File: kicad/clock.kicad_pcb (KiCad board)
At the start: 2 copper layers, 74 x 36 mm, 50 parts, among them P1 CONN_01X03, SW1 SWITCH_MIN, SW2 SWITCH_HR, U1 74LS90, U10 74LS247, U11 74LS73, U2 74LS90, U3 MAX6817, U4 74LS90, U5 74LS247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

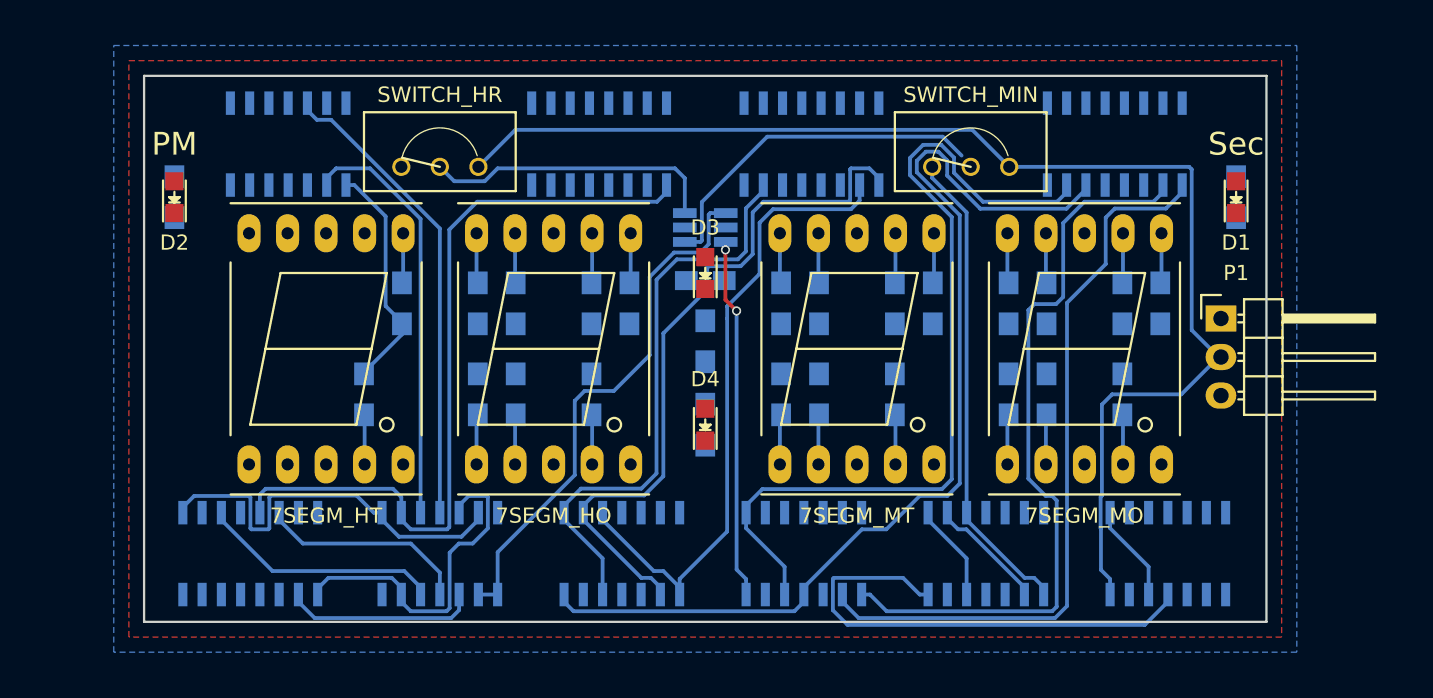
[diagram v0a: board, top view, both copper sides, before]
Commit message: Continue routing, add two layers
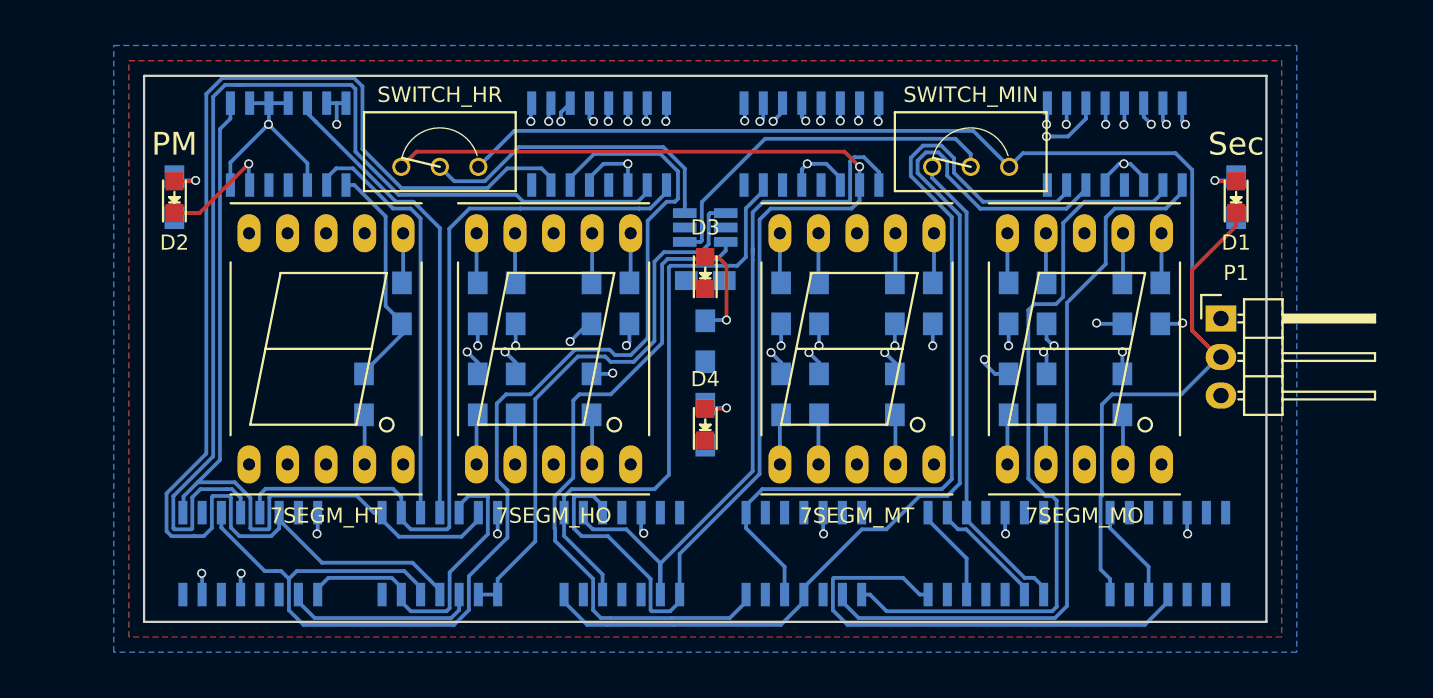
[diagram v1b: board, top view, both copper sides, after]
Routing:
- net /hoi2: track 0.00 -> 73.1 mm
- net /hoi0: track 14.4 -> 86.9 mm
- net /hoi3: track 15.9 -> 79.2 mm
- net VCC: track 0.00 -> 44.2 mm, vias 0 -> 15
- net /mti2: track 42.8 -> 84.2 mm, vias 0 -> 1
- net /hr_one_c: track 0.00 -> 36.5 mm, vias 0 -> 2
- net /min_ten_c: track 0.00 -> 33.1 mm, vias 0 -> 2
- net /min_one_c: track 0.00 -> 32.1 mm, vias 0 -> 2
- net /hr_one_g: track 0.00 -> 30.0 mm, vias 0 -> 2
- net /min_one_g: track 0.00 -> 29.6 mm, vias 0 -> 2
- net /min_ten_g: track 0.00 -> 28.3 mm, vias 0 -> 2
- net Net-(U11-Pad1): track 26.7 -> 54.1 mm
- net /hr_one_d: track 0.00 -> 27.0 mm, vias 0 -> 2
- net /min_ten_d: track 0.00 -> 25.1 mm, vias 0 -> 2
- net /min_ten_f: track 0.00 -> 24.9 mm, vias 0 -> 2
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- added copper zone on In1.Cu, net GND
- added copper zone on In2.Cu, net GND
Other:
- copper layers 2 -> 4

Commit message: Add bypass caps and route VCC
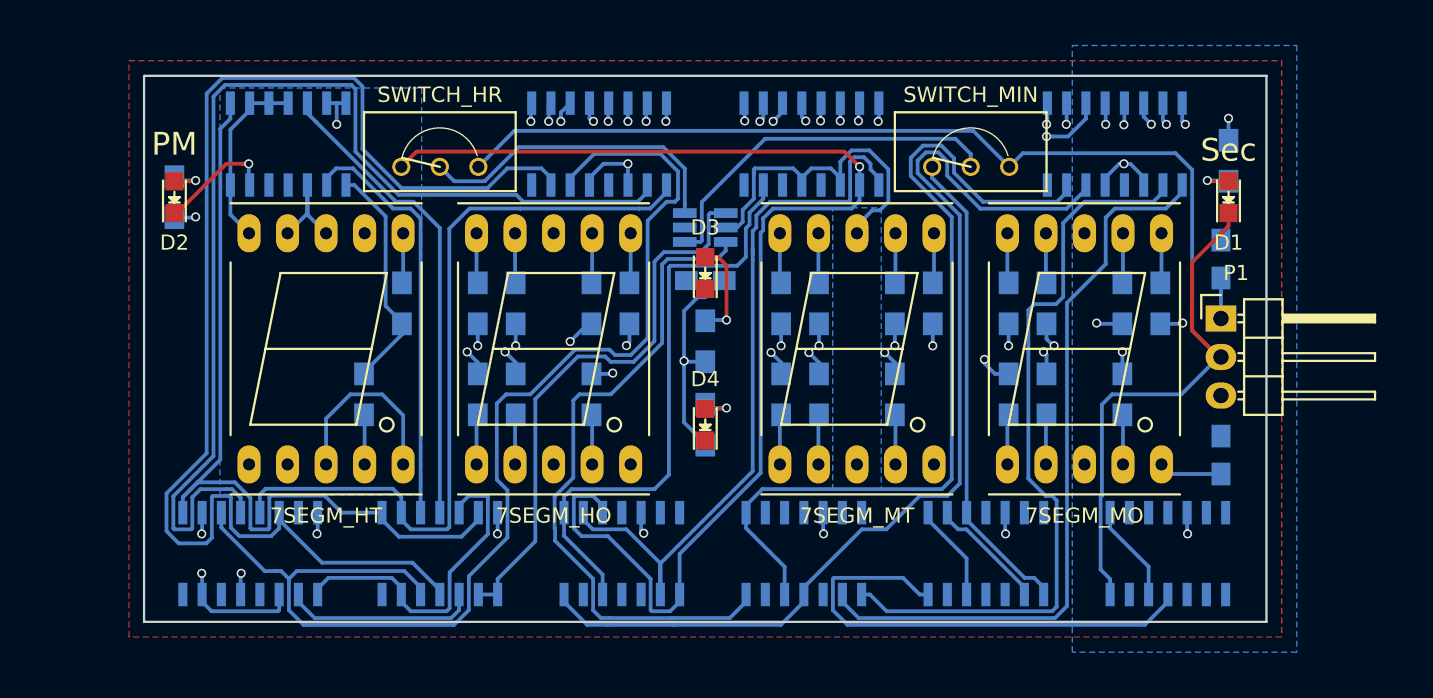
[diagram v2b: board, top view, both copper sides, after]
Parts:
- added C1: 22μF, Capacitors_SMD:C_0805_HandSoldering, B.Cu at (189.0, 103.0)
- added C2: 22μF, Capacitors_SMD:C_0805_HandSoldering, B.Cu at (189.0, 90.1)
- moved R1 2.45 mm to (189.5, 83.6), turned to 90 degrees
- moved D1 0.50 mm to (189.5, 86.0)
- renumbered C1 to C3, U8 to U7, U7 to U8
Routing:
- net VCC: track 44.2 -> 114.3 mm, vias 15 -> 17
- net /osc: track 96.5 -> 98.2 mm
- net Net-(U11-Pad1): track 54.1 -> 55.7 mm
- net /hoi0: track 86.9 -> 87.6 mm
- added copper zone on B.Cu, net VCC

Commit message: Complete layout, pass DRC, create gerbers
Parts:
- added REF**: MountingHole_3.2mm_M3, Mounting_Holes:MountingHole_3.2mm_M3, F.Cu at (194.5, 111.0)
- added REF**: MountingHole_3.2mm_M3, Mounting_Holes:MountingHole_3.2mm_M3, F.Cu at (116.0, 111.0)
- added REF**: MountingHole_3.2mm_M3, Mounting_Holes:MountingHole_3.2mm_M3, F.Cu at (116.0, 81.0)
- added REF**: MountingHole_3.2mm_M3, Mounting_Holes:MountingHole_3.2mm_M3, F.Cu at (194.5, 81.0)
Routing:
- net GND: track 1.41 -> 63.7 mm, vias 1 -> 14
- net /mti2: track 84.1 -> 91.8 mm
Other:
- board size 74 x 36 mm -> 86.5 x 38 mm
- net class Default: clearance 0.2 -> 0.16
- rule trace_clearance: 0.2 -> 0.16

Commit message: Add version and license silkscreen text
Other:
- board text added: "Click-Clock Board v0.1 GNU GPLv3"
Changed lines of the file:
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@@
     (links 179)
     (no_connects 0)
-    (area 106.482857 73 204.017143 119.000001)
+    (area 111.924999 76.924999 198.575001 115.075001)
     (thickness 1.6)
-    (drawings 18)
+    (drawings 19)
     (tracks 993)
     (zones 0)
@@
       (net 2 GND) (zone_connect 2))
   )
+  (gr_text "Click-Clock Board v0.1\nGNU GPLv3" (at 155 111) (layer F.SilkS)
+    (effects (font (size 1.5 1.5) (thickness 0.3)))
+  )
   (gr_line (start 116 77) (end 194.5 77) (angle 90) (layer Edge.Cuts) (width 0.15))

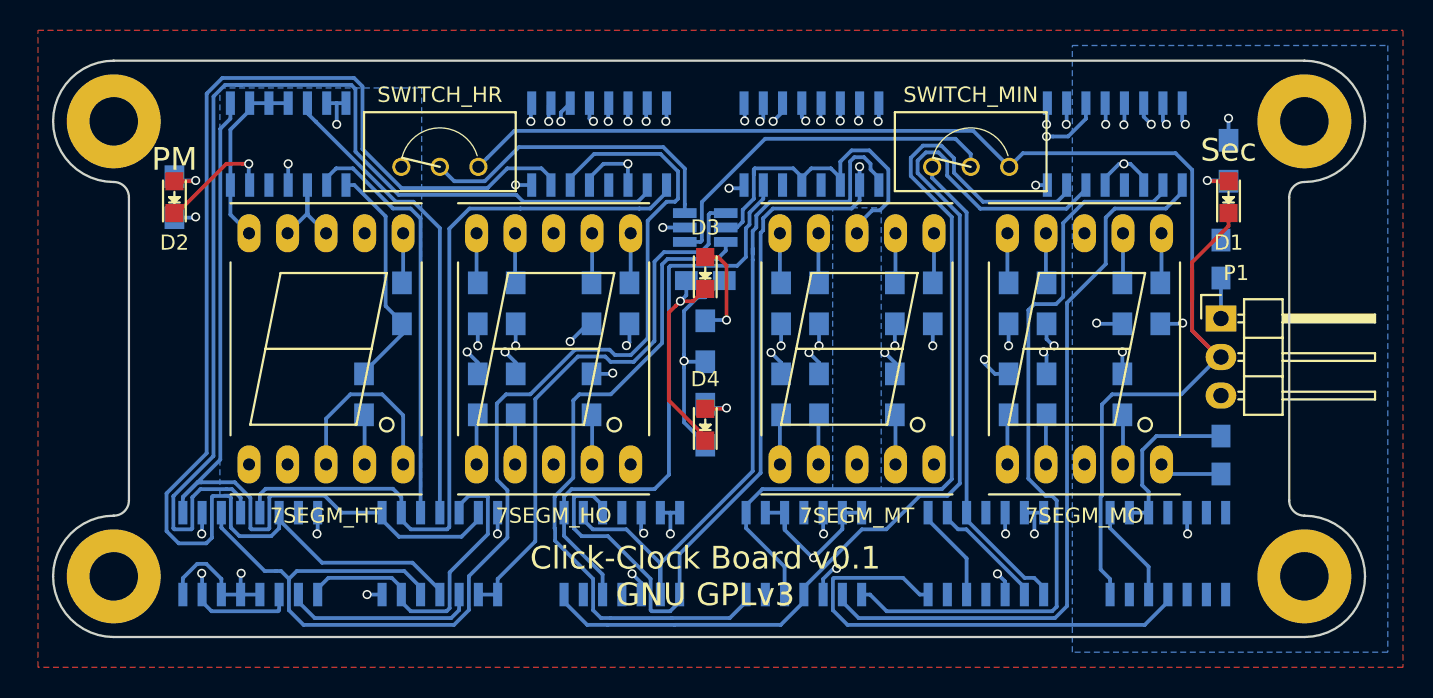
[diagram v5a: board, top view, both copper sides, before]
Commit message: Realign components and make the board more symmetric
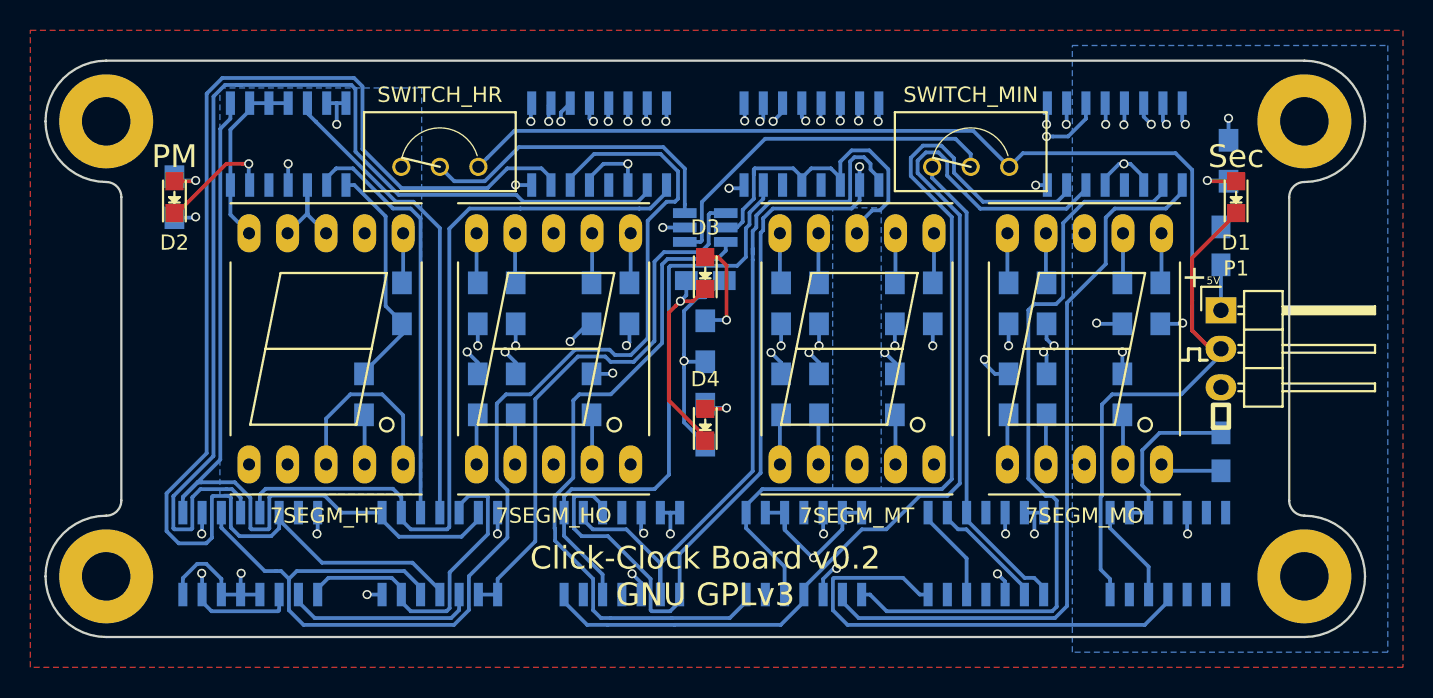
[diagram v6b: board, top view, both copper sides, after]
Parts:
- moved C2 0.87 mm to (189.0, 89.2)
- moved P1 0.54 mm to (189.0, 93.5)
- moved D1 0.50 mm to (190.0, 86.0)
- moved REF** 0.50 mm to (115.5, 111.0)
- moved REF** 0.50 mm to (115.5, 81.0)
- moved C1 0.21 mm to (189.0, 102.8)
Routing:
- net VCC: track 114.3 -> 115.4 mm
- net /osc: track 98.2 -> 99.2 mm
- net Net-(D1-Pad2): track 3.20 -> 3.70 mm
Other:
- board size 86.5 x 38 mm -> 87 x 38 mm
- board text added: "+"
- board text added: "5V"
- board text added: "Click-Clock Board v0.2 GNU GPLv3"
- board text added: "⏚"
- board text removed: "Click-Clock Board v0.1 GNU GPLv3"

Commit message: Optimize tack and via placement
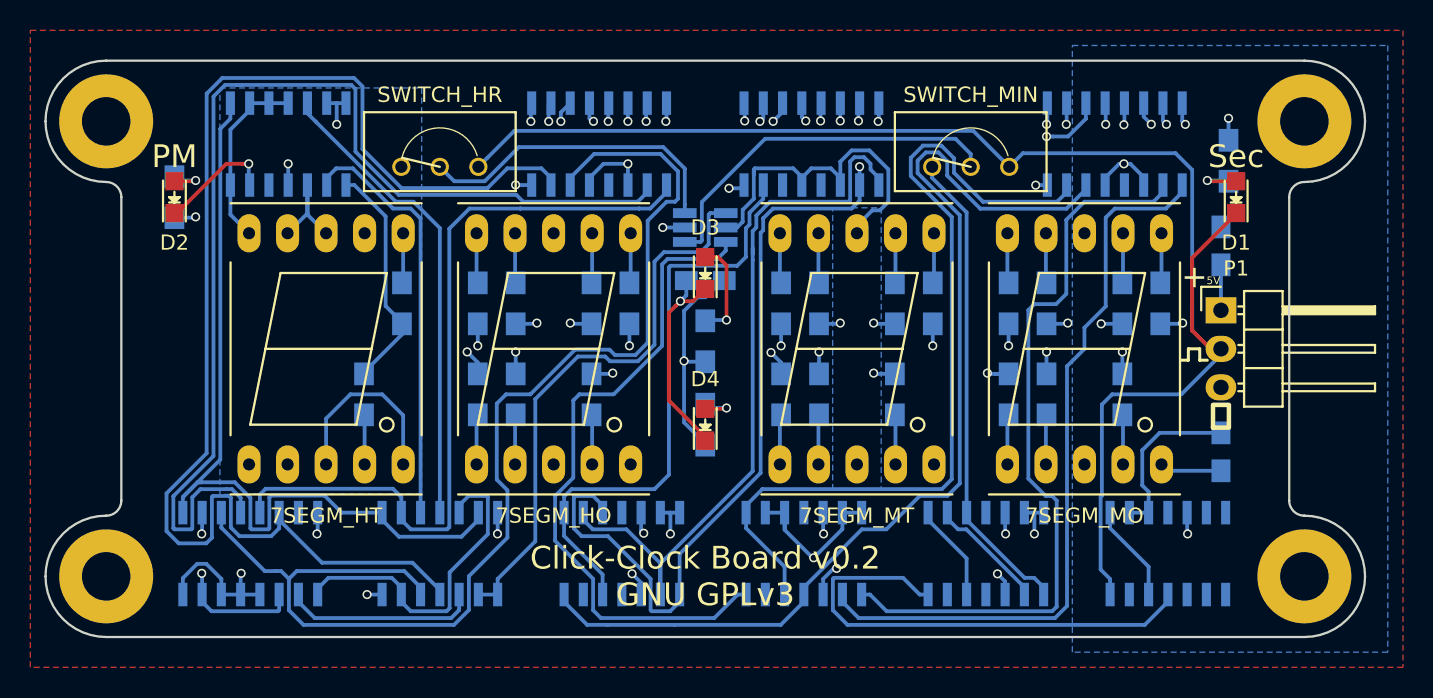
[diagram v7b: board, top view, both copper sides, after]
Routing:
- net /min_one_f: track 24.6 -> 22.5 mm
- net /hr_one_f: track 24.9 -> 22.9 mm
- net /min_ten_a: track 22.5 -> 20.4 mm
- net /hr_one_a: track 20.3 -> 18.9 mm
- net /min_one_e: track 22.2 -> 23.7 mm
- net /min_ten_f: track 24.9 -> 23.6 mm
- net /min_ten_d: track 25.1 -> 26.3 mm
- net /hr_one_d: track 27.0 -> 28.1 mm
- net /min_ten_c: track 33.1 -> 32.4 mm
- net /min_one_d: track 23.3 -> 24.0 mm
